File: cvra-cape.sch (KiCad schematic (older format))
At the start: 27 parts

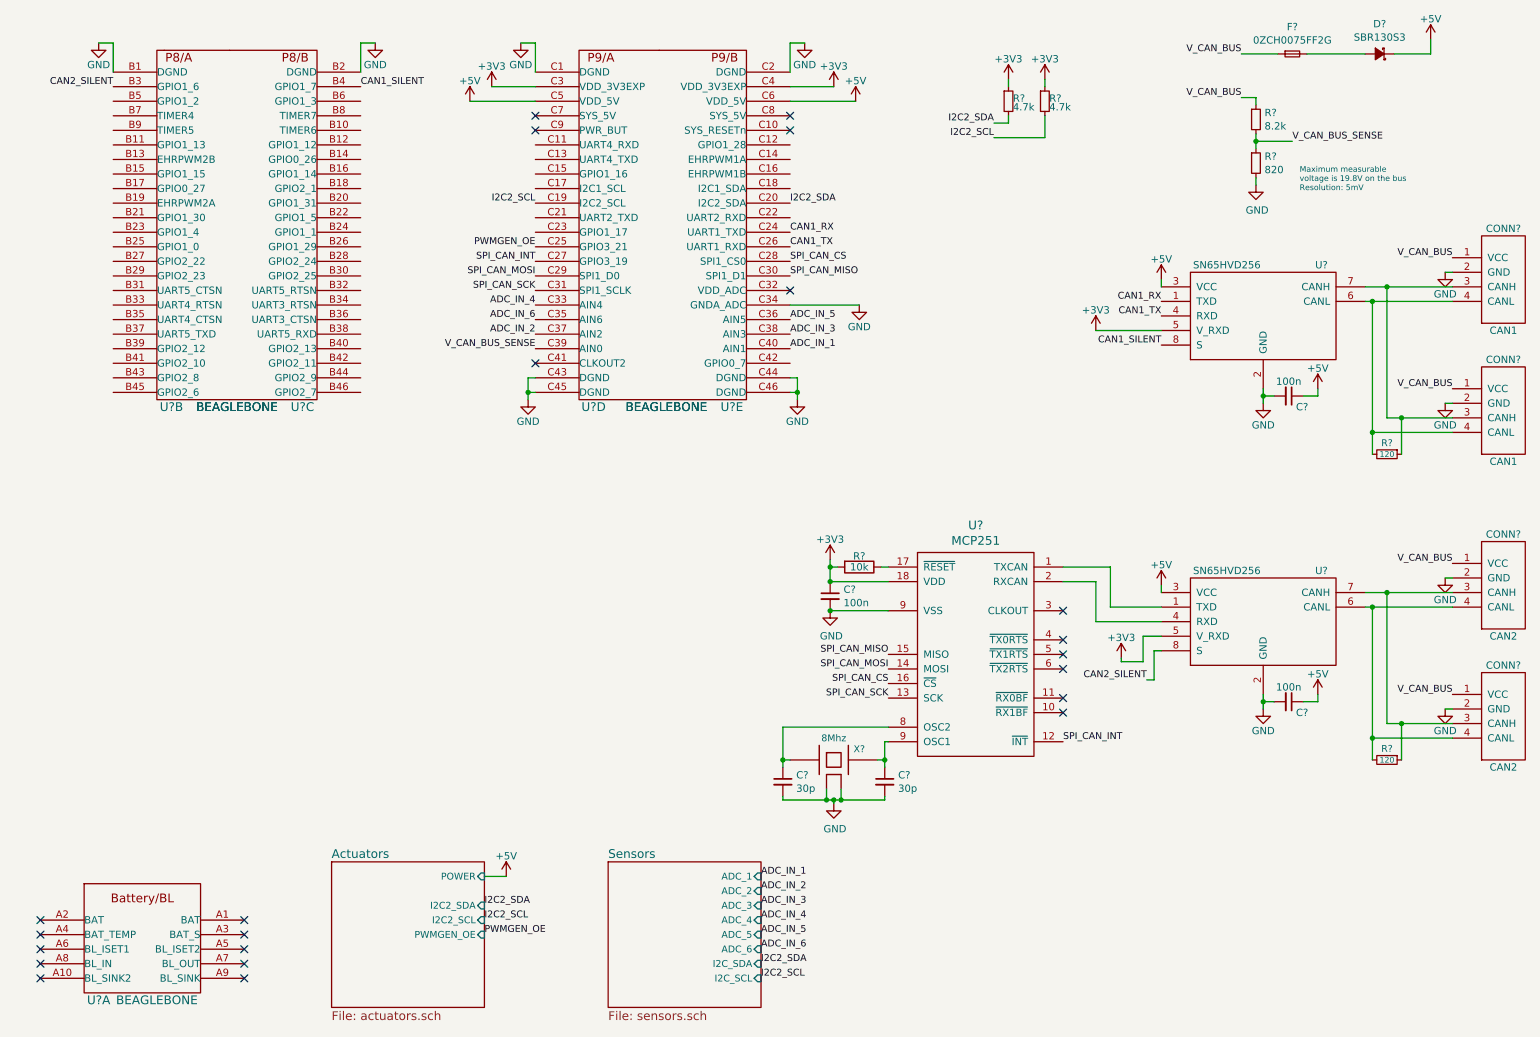
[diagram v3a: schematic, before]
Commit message: Add digital inputs with power option
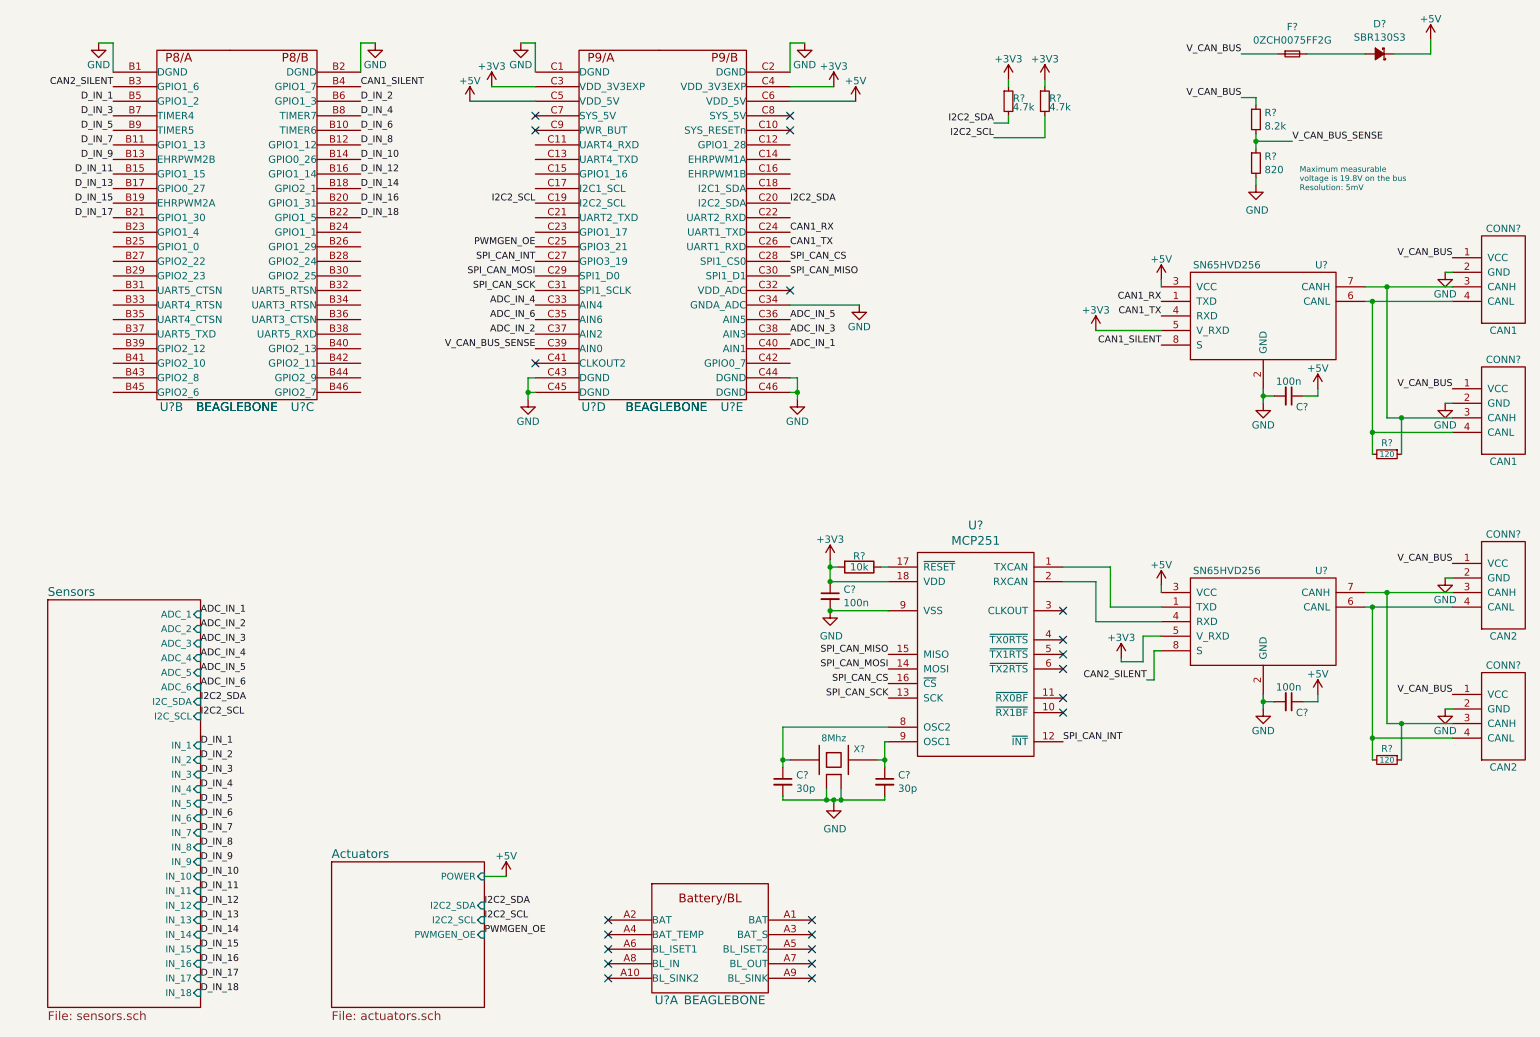
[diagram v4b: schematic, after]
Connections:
- net D_IN_7: now reaches U?.B11 (GPIO1_13)
- net D_IN_9: now reaches U?.B13 (EHRPWM2B)
- net D_IN_11: now reaches U?.B15 (GPIO1_15)
- net D_IN_13: now reaches U?.B17 (GPIO0_27)
- net D_IN_15: now reaches U?.B19 (EHRPWM2A)
- net D_IN_17: now reaches U?.B21 (GPIO1_30)
- net D_IN_1: now reaches U?.B5 (GPIO1_2)
- net D_IN_3: now reaches U?.B7 (TIMER4)
- net D_IN_5: now reaches U?.B9 (TIMER5)
- net D_IN_6: now reaches U?.B10 (TIMER6)
- net D_IN_8: now reaches U?.B12 (GPIO1_12)
- net D_IN_10: now reaches U?.B14 (GPIO0_26)
- net D_IN_12: now reaches U?.B16 (GPIO1_14)
- net D_IN_14: now reaches U?.B18 (GPIO2_1)
- net D_IN_16: now reaches U?.B20 (GPIO1_31)
- net D_IN_18: now reaches U?.B22 (GPIO1_5)
- net D_IN_2: now reaches U?.B6 (GPIO1_3)
- net D_IN_4: now reaches U?.B8 (TIMER7)
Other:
- moved on the sheet: U?A
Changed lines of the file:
@@
 L BEAGLEBONE U?
 U 1 1 5630E650
-P 1150 7450
-F 0 "U?" H 1200 7400 60  0000 C CNN
-F 1 "BEAGLEBONE" H 1600 7400 60  0000 C CNN
-F 2 "" H 1150 7450 60  0000 C CNN
-F 3 "" H 1150 7450 60  0000 C CNN
-	1    1150 7450
+P 5050 7450
+F 0 "U?" H 5100 7400 60  0000 C CNN
+F 1 "BEAGLEBONE" H 5500 7400 60  0000 C CNN
+F 2 "" H 5050 7450 60  0000 C CNN
+F 3 "" H 5050 7450 60  0000 C CNN
+	1    5050 7450
 	1    0    0    -1
 $EndComp
@@
 	1    0    0    -1
 $EndComp
-NoConn ~ 2200 6950
-NoConn ~ 2200 7050
-NoConn ~ 2200 7150
-NoConn ~ 2200 7250
-NoConn ~ 2200 7350
-NoConn ~ 800  7350
-NoConn ~ 800  7250
-NoConn ~ 800  7150
-NoConn ~ 800  7050
-NoConn ~ 800  6950
+NoConn ~ 6100 6950
+NoConn ~ 6100 7050
+NoConn ~ 6100 7150
+NoConn ~ 6100 7250
+NoConn ~ 6100 7350
+NoConn ~ 4700 7350
+NoConn ~ 4700 7250
+NoConn ~ 4700 7150
+NoConn ~ 4700 7050
+NoConn ~ 4700 6950
 $Comp
 L SN65HVD256 U?
@@
 I2C2_SDA
 $Sheet
-S 4700 6550 1050 1000
+S 850  4750 1050 2800
 U 569FF03E
 F0 "Sensors" 60
 F1 "sensors.sch" 60
-F2 "ADC_1" I R 5750 6650 47
-F3 "ADC_2" I R 5750 6750 47
-F4 "ADC_3" I R 5750 6850 47
-F5 "ADC_4" I R 5750 6950 47
-F6 "ADC_5" I R 5750 7050 47
-F7 "ADC_6" I R 5750 7150 47
-F8 "I2C_SCL" I R 5750 7350 47
-F9 "I2C_SDA" I R 5750 7250 47
+F2 "ADC_1" I R 1900 4850 47
+F3 "ADC_2" I R 1900 4950 47
+F4 "ADC_3" I R 1900 5050 47
+F5 "ADC_4" I R 1900 5150 47
+F6 "ADC_5" I R 1900 5250 47
+F7 "ADC_6" I R 1900 5350 47
+F8 "I2C_SCL" I R 1900 5550 47
+F9 "I2C_SDA" I R 1900 5450 47
+F10 "IN_1" I R 1900 5750 47
+F11 "IN_2" I R 1900 5850 47
+F12 "IN_3" I R 1900 5950 47
+F13 "IN_4" I R 1900 6050 47
+F14 "IN_5" I R 1900 6150 47
+F15 "IN_6" I R 1900 6250 47
+F16 "IN_7" I R 1900 6350 47
+F17 "IN_8" I R 1900 6450 47
+F18 "IN_9" I R 1900 6550 47
+F19 "IN_10" I R 1900 6650 47
+F20 "IN_11" I R 1900 6750 47
+F21 "IN_12" I R 1900 6850 47
+F22 "IN_13" I R 1900 6950 47
+F23 "IN_14" I R 1900 7050 47
+F24 "IN_15" I R 1900 7150 47
+F25 "IN_16" I R 1900 7250 47
+F26 "IN_17" I R 1900 7350 47
+F27 "IN_18" I R 1900 7450 47
 $EndSheet
-Text Label 5750 6650 0    47   ~ 0
+Text Label 1900 4850 0    47   ~ 0
 ADC_IN_1
-Text Label 5750 6850 0    47   ~ 0
+Text Label 1900 5050 0    47   ~ 0
 ADC_IN_3
-Text Label 5750 7050 0    47   ~ 0
+Text Label 1900 5250 0    47   ~ 0
 ADC_IN_5
-Text Label 5750 6750 0    47   ~ 0
+Text Label 1900 4950 0    47   ~ 0
 ADC_IN_2
-Text Label 5750 6950 0    47   ~ 0
+Text Label 1900 5150 0    47   ~ 0
 ADC_IN_4
-Text Label 5750 7150 0    47   ~ 0
+Text Label 1900 5350 0    47   ~ 0
 ADC_IN_6
 $Comp
@@
 	5950 925  5950 1125
 Wire Wire Line
-	6000 3225 6000 3325
-Wire Wire Line
-	6000 3325 6000 3375
+	6000 3225 6000 3375
 Wire Wire Line
 	6000 3325 5950 3325
@@
 	4200 3325 4150 3325
 Wire Wire Line
-	4150 3225 4150 3325
-Wire Wire Line
-	4150 3325 4150 3375
+	4150 3225 4150 3375
 Wire Wire Line
 	4150 3225 4200 3225
 Connection ~ 4150 3325
 Wire Wire Line
-	9900 2600 10050 2600
-Wire Wire Line
-	10050 2600 10500 2600
-Wire Wire Line
-	9900 2700 9950 2700
-Wire Wire Line
-	9950 2700 10500 2700
+	9900 2600 10500 2600
+Wire Wire Line
+	9900 2700 10500 2700
 Wire Wire Line
 	10450 2500 10500 2500
@@
 	10450 3400 10500 3400
 Wire Wire Line
-	10050 3500 10150 3500
-Wire Wire Line
-	10150 3500 10500 3500
+	10050 3500 10500 3500
 Wire Wire Line
 	10050 3500 10050 2600
 Connection ~ 10050 2600
 Wire Wire Line
-	9950 2700 9950 3600
-Wire Wire Line
-	9950 3600 9950 3750
+	9950 2700 9950 3750
 Wire Wire Line
 	9950 3600 10500 3600
@@
 	9150 1300 9150 1350
 Wire Wire Line
-	9150 1550 9150 1600
-Wire Wire Line
-	9150 1600 9150 1650
+	9150 1550 9150 1650
 Wire Wire Line
 	9150 1600 9400 1600
@@
 	6400 1325 5950 1325
 Wire Wire Line
-	9900 4700 10050 4700
-Wire Wire Line
-	10050 4700 10500 4700
-Wire Wire Line
-	9900 4800 9950 4800
-Wire Wire Line
-	9950 4800 10500 4800
+	9900 4700 10500 4700
+Wire Wire Line
+	9900 4800 10500 4800
 Wire Wire Line
 	10450 4600 10500 4600
@@
 	10450 5500 10500 5500
 Wire Wire Line
-	10050 5600 10150 5600
-Wire Wire Line
-	10150 5600 10500 5600
+	10050 5600 10500 5600
 Wire Wire Line
 	10050 5600 10050 4700
 Connection ~ 10050 4700
 Wire Wire Line
-	9950 4800 9950 5700
-Wire Wire Line
-	9950 5700 9950 5850
+	9950 4800 9950 5850
 Wire Wire Line
 	9950 5700 10500 5700
@@
 	6200 6050 6200 6125
 Wire Wire Line
-	5900 6125 6200 6125
-Wire Wire Line
-	6200 6125 6250 6125
-Wire Wire Line
-	6250 6125 6300 6125
-Wire Wire Line
-	6300 6125 6600 6125
+	5900 6125 6600 6125
 Wire Wire Line
 	5900 6125 5900 6100
 Wire Wire Line
-	5900 5625 5900 5850
-Wire Wire Line
-	5900 5850 5900 5900
+	5900 5625 5900 5900
 Wire Wire Line
 	5900 5850 5950 5850
@@
 	6550 5850 6600 5850
 Wire Wire Line
-	6600 5725 6600 5850
-Wire Wire Line
-	6600 5850 6600 5900
+	6600 5725 6600 5900
 Wire Wire Line
 	6300 6125 6300 6050
@@
 	8050 4900 8500 4900
 Wire Wire Line
-	6225 4475 6225 4525
-Wire Wire Line
-	6225 4525 6225 4625
+	6225 4475 6225 4625
 $Comp
 L R R?
@@
 SPI_CAN_SCK
 Wire Wire Line
-	9200 3300 9200 3350
-Wire Wire Line
-	9200 3350 9200 3400
+	9200 3300 9200 3400
 Wire Wire Line
 	9200 3350 9275 3350
@@
 $EndComp
 Wire Wire Line
-	9200 5400 9200 5450
-Wire Wire Line
-	9200 5450 9200 5500
+	9200 5400 9200 5500
 Wire Wire Line
 	9200 5450 9275 5450
@@
 Wire Wire Line
 	4000 6650 3850 6650
-Text Label 5750 7250 0    47   ~ 0
+Text Label 1900 5450 0    47   ~ 0
 I2C2_SDA
-Text Label 5750 7350 0    47   ~ 0
+Text Label 1900 5550 0    47   ~ 0
 I2C2_SCL
+Text Label 1900 5750 0    47   ~ 0
+D_IN_1
+Text Label 1900 5850 0    47   ~ 0
+D_IN_2
+Text Label 1900 5950 0    47   ~ 0
+D_IN_3
+Text Label 1900 6050 0    47   ~ 0
+D_IN_4
+Text Label 1900 6150 0    47   ~ 0
+D_IN_5
+Text Label 1900 6250 0    47   ~ 0
+D_IN_6
+Text Label 1900 6350 0    47   ~ 0
+D_IN_7
+Text Label 1900 6450 0    47   ~ 0
+D_IN_8
+Text Label 1900 6550 0    47   ~ 0
+D_IN_9
+Text Label 1900 6650 0    47   ~ 0
+D_IN_10
+Text Label 1900 6750 0    47   ~ 0
+D_IN_11
+Text Label 1900 6850 0    47   ~ 0
+D_IN_12
+Text Label 1900 6950 0    47   ~ 0
+D_IN_13
+Text Label 1900 7050 0    47   ~ 0
+D_IN_14
+Text Label 1900 7150 0    47   ~ 0
+D_IN_15
+Text Label 1900 7250 0    47   ~ 0
+D_IN_16
+Text Label 1900 7350 0    47   ~ 0
+D_IN_17
+Text Label 1900 7450 0    47   ~ 0
+D_IN_18
+Text Label 1300 1325 2    47   ~ 0
+D_IN_1
+Text Label 3000 1325 0    47   ~ 0
+D_IN_2
+Text Label 1300 1425 2    47   ~ 0
+D_IN_3
+Text Label 3000 1425 0    47   ~ 0
+D_IN_4
+Text Label 1300 1525 2    47   ~ 0
+D_IN_5
+Text Label 3000 1525 0    47   ~ 0
+D_IN_6
+Text Label 1300 1625 2    47   ~ 0
+D_IN_7
+Text Label 3000 1625 0    47   ~ 0
+D_IN_8
+Text Label 1300 1725 2    47   ~ 0
+D_IN_9
+Text Label 3000 1725 0    47   ~ 0
+D_IN_10
+Text Label 1300 1825 2    47   ~ 0
+D_IN_11
+Text Label 3000 1825 0    47   ~ 0
+D_IN_12
+Text Label 1300 1925 2    47   ~ 0
+D_IN_13
+Text Label 3000 1925 0    47   ~ 0
+D_IN_14
+Text Label 1300 2025 2    47   ~ 0
+D_IN_15
+Text Label 3000 2025 0    47   ~ 0
+D_IN_16
+Text Label 1300 2125 2    47   ~ 0
+D_IN_17
+Text Label 3000 2125 0    47   ~ 0
+D_IN_18
 $EndSCHEMATC
